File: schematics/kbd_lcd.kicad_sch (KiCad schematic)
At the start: 44 parts, among them J2 Mini-DIN-6, Q1 2N3906, U1 74HC04, U12 74HC04, U13 74HC125, U14 74HC14, U15 NE555P, U16 74HC04, U17 74HC595, U18 80x4 Character LCD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

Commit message: i can type lowercase! added tab key support and fixed cr and lf
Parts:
- removed R32: 10kΩ, symbol Device:R
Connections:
- net GND: now also R26.2, R27.1, R28.1
- net VCC: no longer R26.1, R27.1, R28.2
- net at U13.13, U14.5, U17.13 (~{OE})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: now also R28.2; no longer R28.1
- net at U20.18 (CB1): now also R26.1; no longer R26.2
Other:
- moved on the sheet: C5, C6, C9, D10, D11, D12, D3, D8, D9, J2, R15, R17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

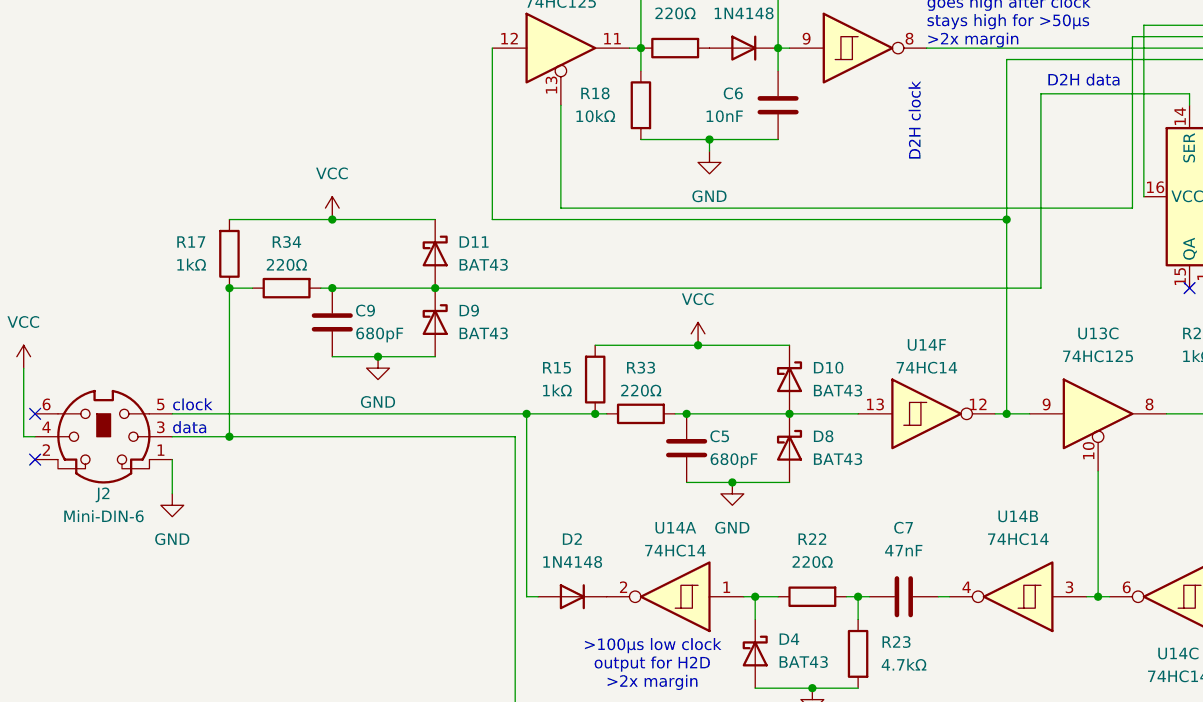
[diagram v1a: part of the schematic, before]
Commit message: trying to make it automatically hold reset during power-on. it's a little better
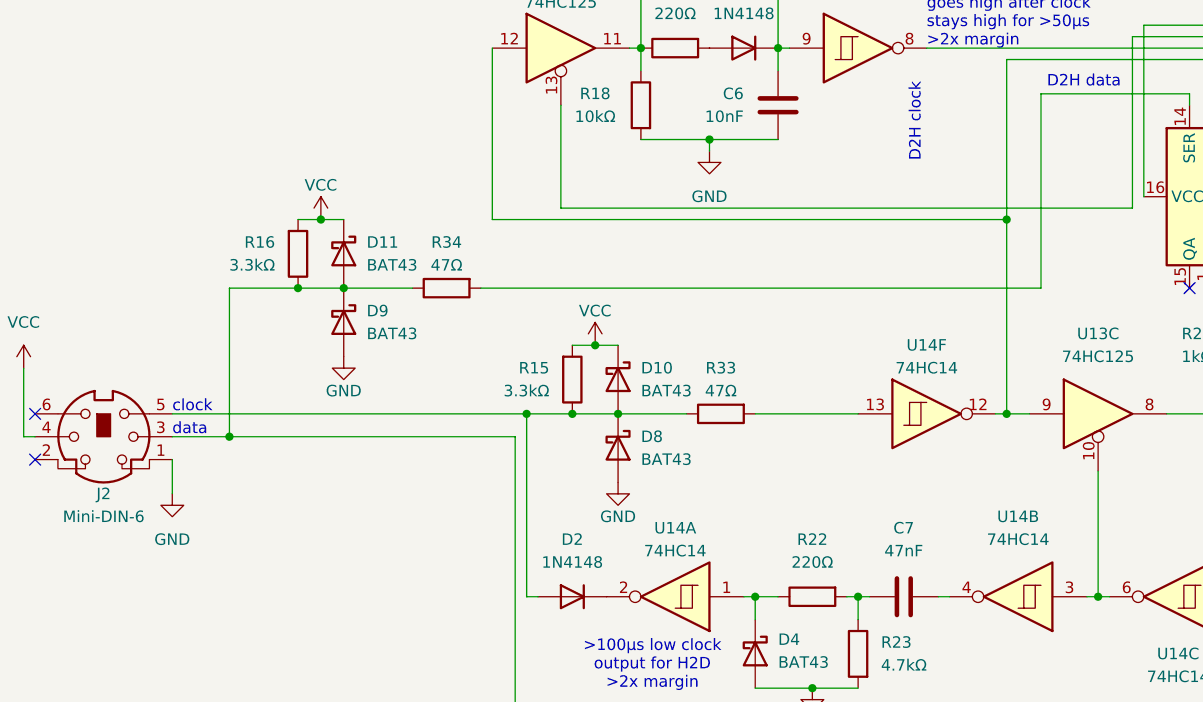
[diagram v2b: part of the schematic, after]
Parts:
- removed C5, C9: 680pF, symbol Device:C
- removed R17: 1kΩ, symbol Device:R
- added R16: 3.3kΩ, symbol Device:R
- R15: value 1kΩ -> 3.3kΩ
- R33, R34: value 220Ω -> 47Ω
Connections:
- net VCC: now also R16.2
- net at R33.2, U14.13: no longer D10.2 (A), D8.1 (K)
- net at D11.2 (A), D9.1 (K): now also D12.2 (A), J2.3, R34.1, R16.1; no longer R34.2, U17.14 (SER)
- net at D2.2 (A), J2.5, R15.1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: now also D10.2 (A), D8.1 (K)
- new net: R34.2, U17.14 (SER)
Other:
- moved on the sheet: R15, R33

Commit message: progress fixing caps lock led
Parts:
- added R31: 10kΩ, symbol Device:R
- R24: value 1kΩ -> 220Ω
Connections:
- net GND: now also R27.2; no longer R27.1, U14.11
- net VCC: now also R31.1
- net at U13.9, U14.12, U17.11 (SRCLK)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: no longer U13.12
- net at R33.2, U14.13: now also U13.12
- net at R18.1, R20.1, R21.1: now also U14.10; no longer U13.11
- net at U20.19 (CB2): now also R27.1; no longer R27.2
- new net: R31.2, U13.11, U14.11
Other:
- moved on the sheet: D11, D9, R16, R25, R26, R27, R34, U13D, U18

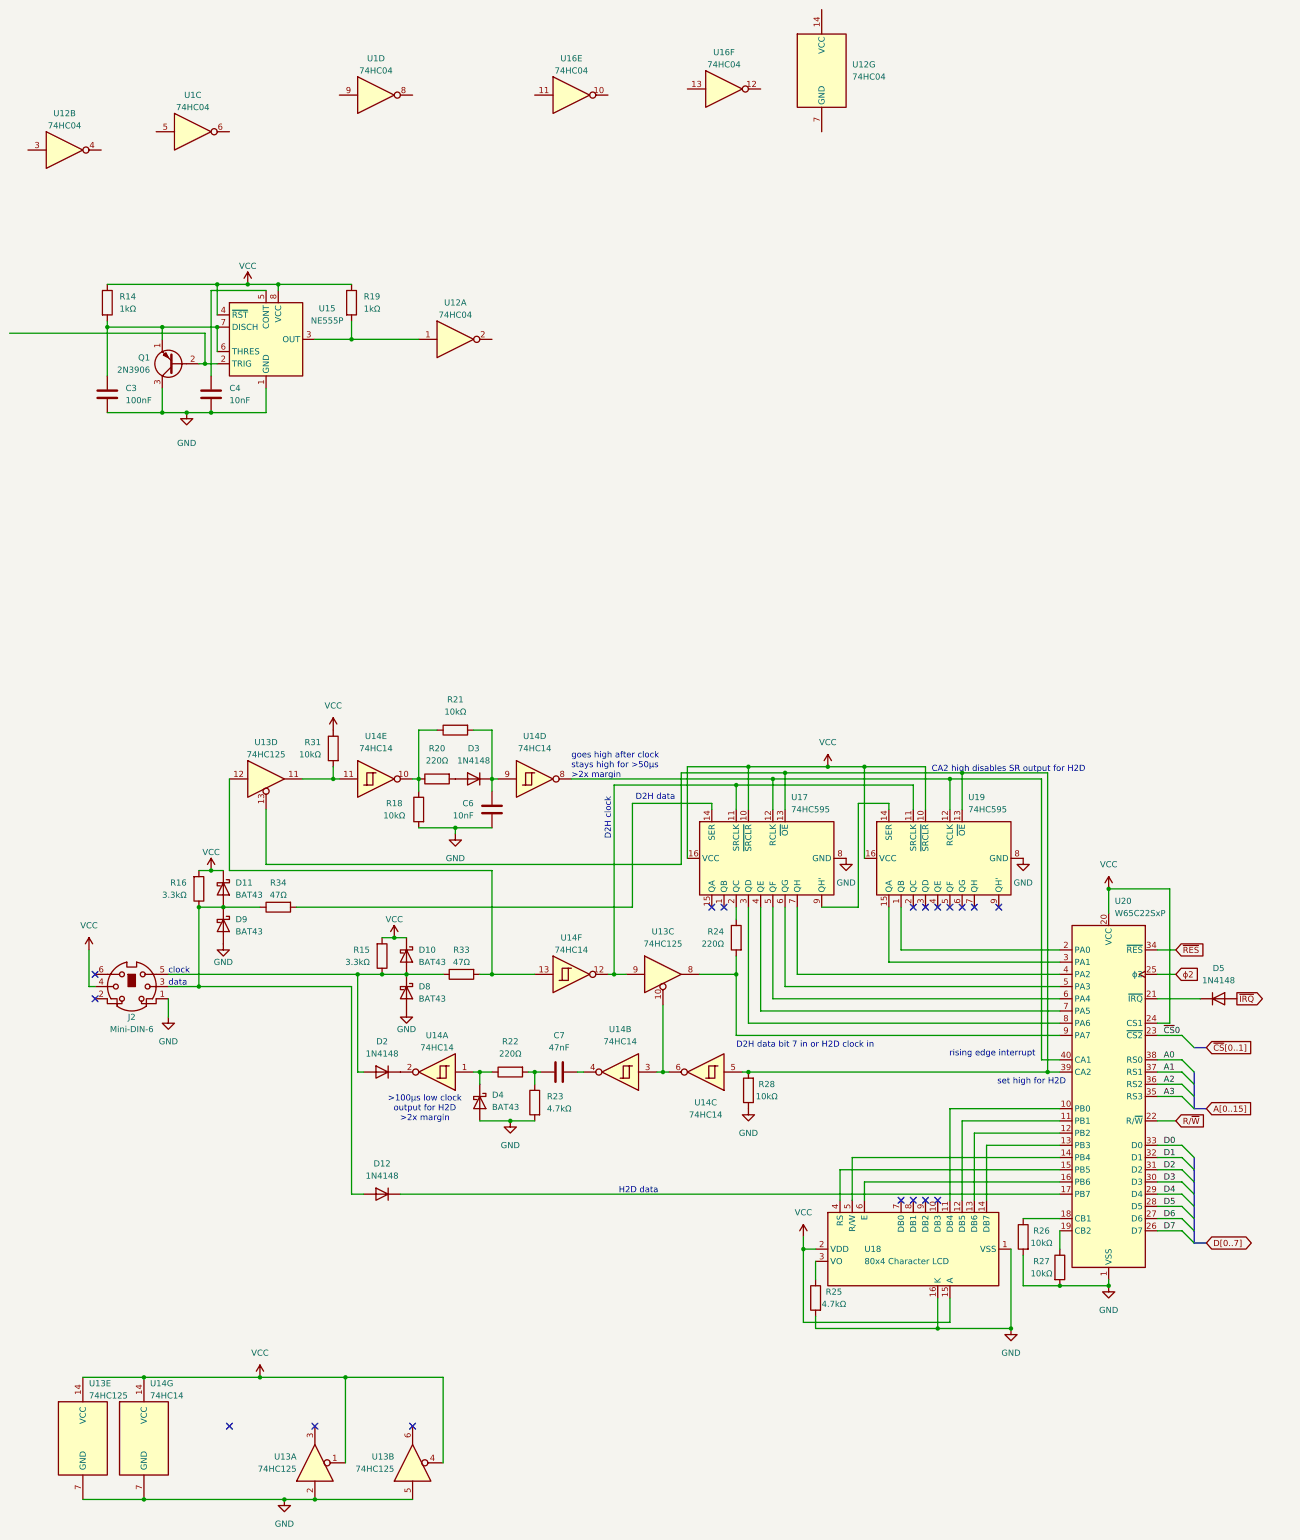
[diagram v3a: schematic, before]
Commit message: rewired the keyboard to remove 74HC245
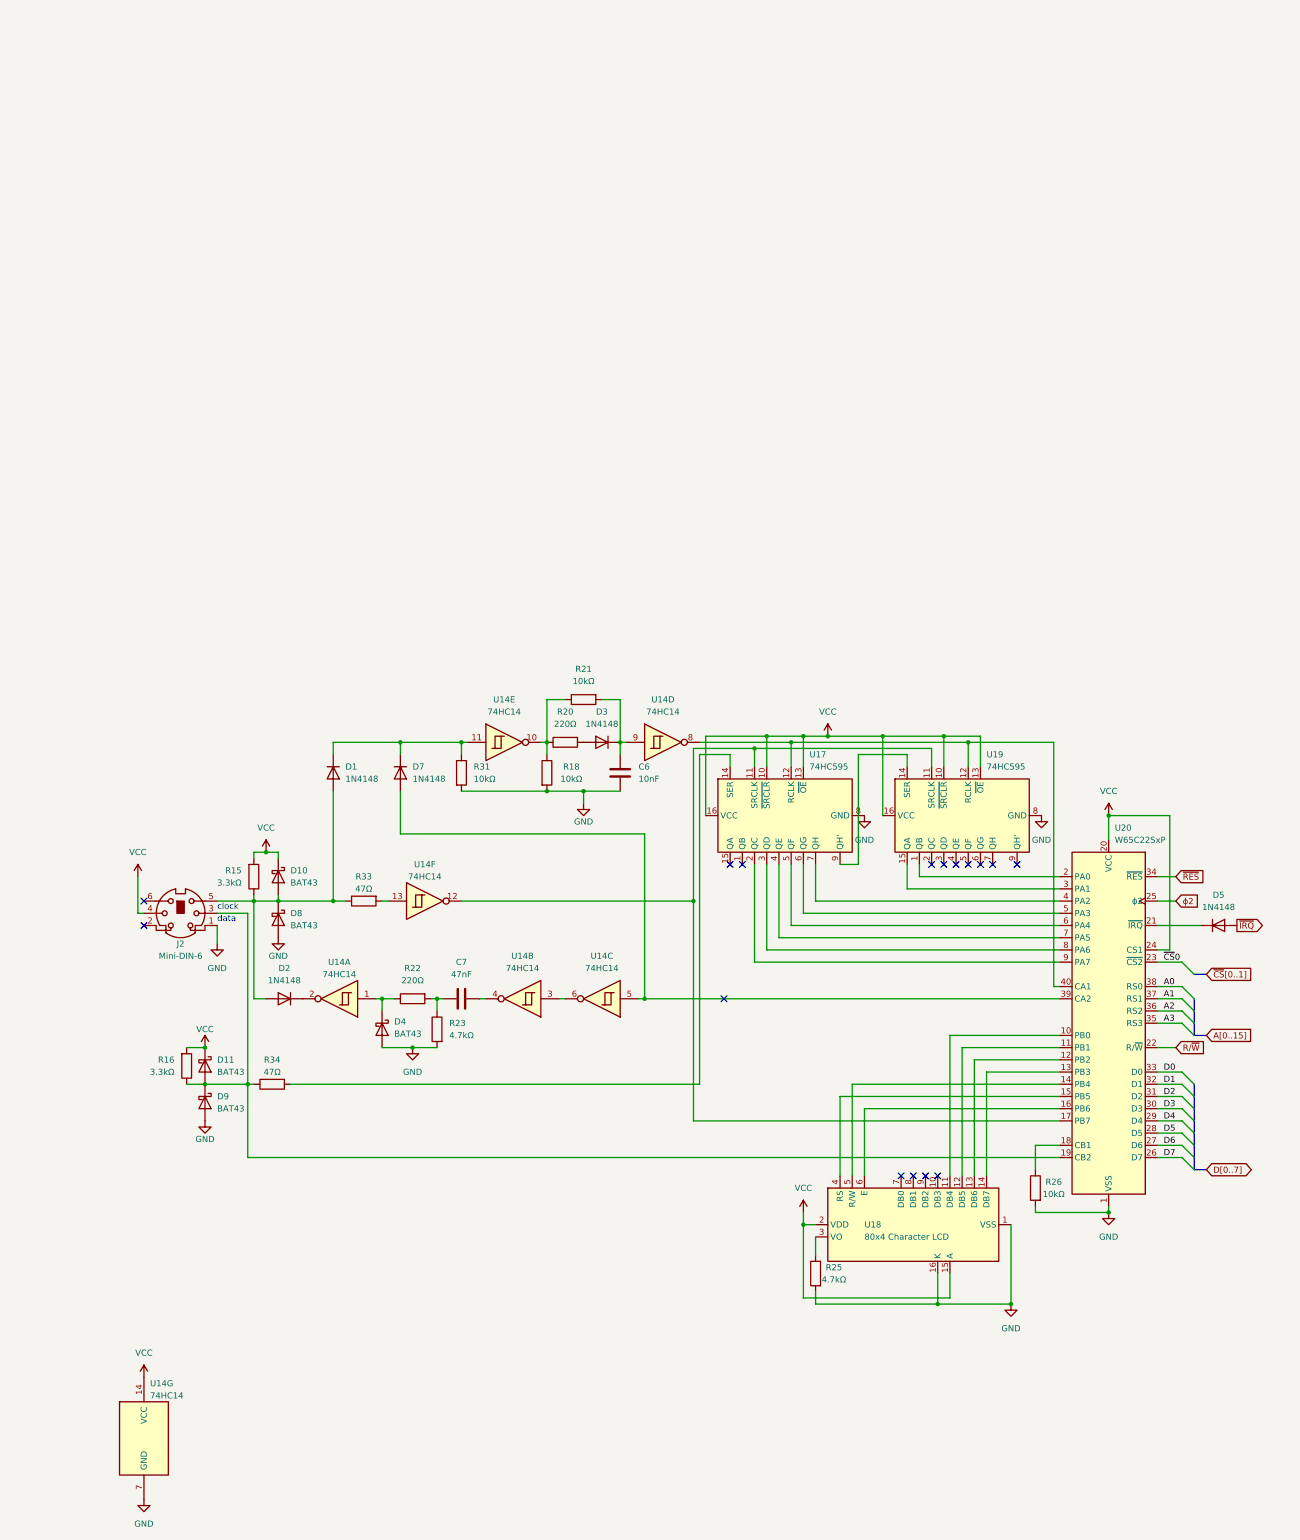
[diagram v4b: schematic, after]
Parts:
- removed C3: 100nF, symbol Device:C
- removed C4: 10nF, symbol Device:C
- removed D12: 1N4148, Diode_THT:D_DO-35_SOD27_P7.62mm_Horizontal, symbol Diode:1N4148
- removed Q1: 2N3906, Package_TO_SOT_THT:TO-92_Inline, symbol Transistor_BJT:2N3906
- removed R14, R19: 1kΩ, symbol Device:R
- removed R24: 220Ω, symbol Device:R
- removed R27, R28: 10kΩ, symbol Device:R
- removed U1, U12, U16: 74HC04, symbol 74xx:74HC04
- removed U13: 74HC125, symbol 74xx:74LS125
- removed U15: NE555P, Package_DIP:DIP-8_W7.62mm, symbol Timer:NE555P
- added D1, D7: 1N4148, Diode_THT:D_DO-35_SOD27_P7.62mm_Horizontal, symbol Diode:1N4148
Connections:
- net GND: now also R31.2
- net VCC: now also U17.13 (~{OE}), U19.13 (~{OE}); no longer R31.1
- net at D11.2 (A), D9.1 (K), J2.3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: now also U20.19 (CB2)
- net at U14.12, U17.11 (SRCLK), U19.11 (SRCLK): now also U20.17 (PB7)
- net at U14.11: now also R31.1, D1.1 (K), D7.1 (K); no longer R31.2
- net at U14.5, U20.39 (CA2): now also D7.2 (A); no longer U17.13 (~{OE}), U19.13 (~{OE})
- net at D10.2 (A), D2.2 (A), D8.1 (K)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: now also D1.2 (A)
- net at U20.9 (PA7): now also U17.2 (QC)
- no-connect marks 18 -> 16
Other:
- note removed: ">100µs low clock output for H2D >2x margin"
- note removed: "CA2 high disables SR output for H2D"
- note removed: "D2H clock"
- note removed: "D2H data"
- note removed: "D2H data bit 7 in or H2D clock in"
- note removed: "H2D data"
- note removed: "goes high after clock stays high for >50µs >2x margin"
- note removed: "rising edge interrupt"
- note removed: "set high for H2D"
- moved on the sheet: C6, C7, D10, D11, D2, D3, D4, D5, D8, D9, J2, R15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

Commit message: Address decoder pld file and no-VIA keyboard schematic and pld file.
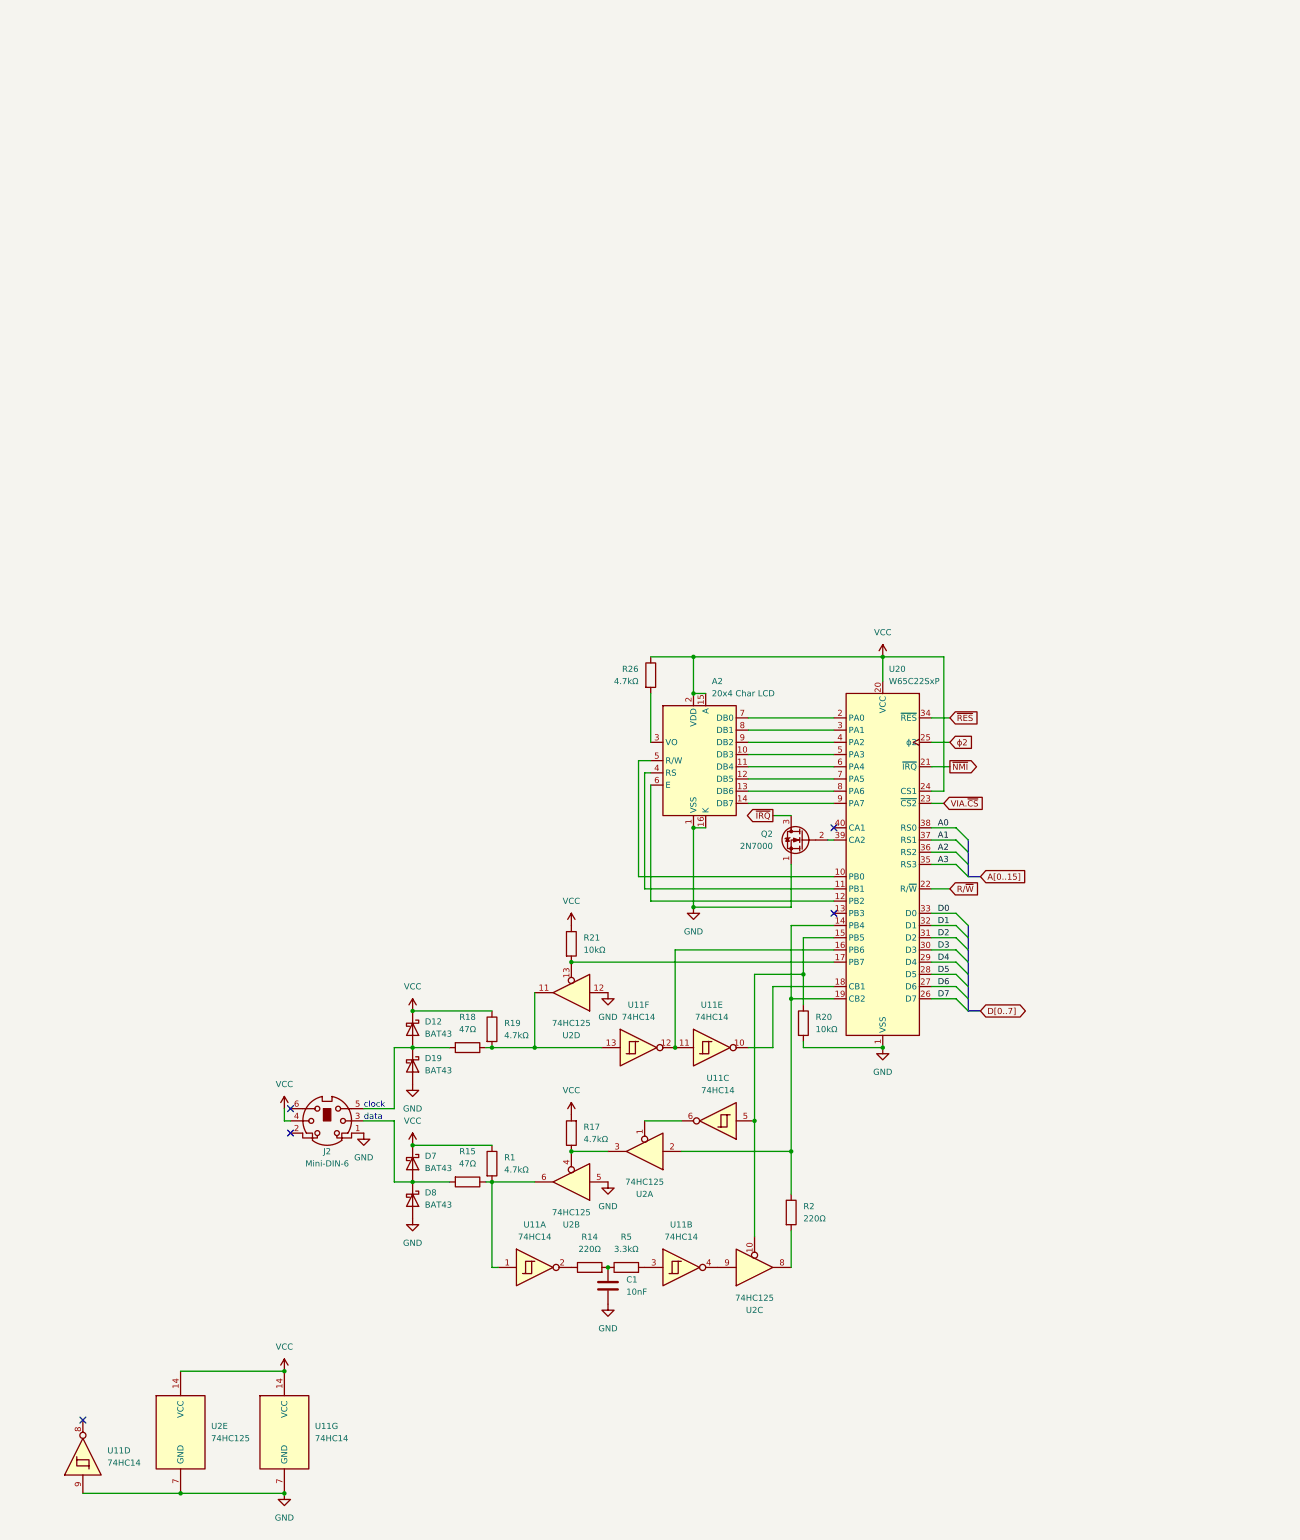
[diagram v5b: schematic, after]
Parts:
- removed C6: 10nF, symbol Device:C
- removed C7: 47nF, symbol Device:C
- removed D1, D2, D3, D5, D7: 1N4148, Diode_THT:D_DO-35_SOD27_P7.62mm_Horizontal, symbol Diode:1N4148
- removed D10, D11, D4, D9: BAT43, Diode_THT:D_DO-35_SOD27_P7.62mm_Horizontal, symbol Diode:BAT43
- removed R16: 3.3kΩ, symbol Device:R
- removed R22: 220Ω, symbol Device:R
- removed R23, R25: 4.7kΩ, symbol Device:R
- removed R31: 10kΩ, symbol Device:R
- removed R33, R34: 47Ω, symbol Device:R
- removed U14: 74HC14, symbol 74xx:74HC14
- removed U17, U19: 74HC595, symbol 74xx:74HC595
- added C1: 10nF, symbol Device:C
- added D12, D19, D7: BAT43, Diode_THT:D_DO-35_SOD27_P7.62mm_Horizontal, symbol Diode:BAT43
- added Q2: 2N7000, Package_TO_SOT_THT:TO-92_Inline, symbol Transistor_FET:2N7000
- added R1, R17, R19: 4.7kΩ, symbol Device:R
- added R14, R2: 220Ω, symbol Device:R
- added R5: 3.3kΩ, symbol Device:R
- added U11: 74HC14, symbol 74xx:74HC14
- added U2: 74HC125, symbol 74xx:74LS125
- A2: renamed from U18; value 80x4 Character LCD -> 20x4 Char LCD
- R15: value 3.3kΩ -> 47Ω
- R18: value 10kΩ -> 47Ω
- R20: value 220Ω -> 10kΩ
- R26: value 10kΩ -> 4.7kΩ
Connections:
- net GND: now also R20.2, C1.2, D19.2 (A), Q2.1 (S), U11.7 (GND), U11.9, U2.12, U2.5, U2.7 (GND); no longer R18.2, R26.2
- net VCC: now also R21.1, R26.1, D12.1 (K), D7.1 (K), R1.1, R17.2, R19.1, U11.14 (VCC), U2.14 (VCC); no longer R15.2
- net ~{IRQ}: now also Q2.3 (D)
- net at J2.3: now also D8.1 (K), R15.2, D7.2 (A); no longer U20.19 (CB2)
- net at U20.17 (PB7): now also R21.2, U2.13
- net at U20.39 (CA2): now also Q2.2 (G)
- net at A2.3 (VO): now also R26.2
- net at U20.10 (PB0): now also A2.5 (R/W); no longer A2.11 (DB4)
- net at U20.11 (PB1): now also A2.4 (RS); no longer A2.12 (DB5)
- net at U20.12 (PB2): now also A2.6 (E); no longer A2.13 (DB6)
- net at U20.13 (PB3): no longer A2.14 (DB7)
- net at U20.14 (PB4): now also U20.19 (CB2), R2.1, U2.2; no longer A2.5 (R/W)
- net at U20.15 (PB5): now also R20.1, U11.5, U2.10; no longer A2.4 (RS)
- net at U20.16 (PB6): now also U11.11, U11.12; no longer A2.6 (E)
- net at U20.18 (CB1): now also U11.10; no longer R26.1
- net at U20.2 (PA0): now also A2.7 (DB0)
- net ~{NMI}: now reaches U20.21 (~{IRQ})
- net at U20.3 (PA1): now also A2.8 (DB1)
- net at U20.4 (PA2): now also A2.9 (DB2)
- net at U20.5 (PA3): now also A2.10 (DB3)
- net at U20.6 (PA4): now also A2.11 (DB4)
- net at U20.7 (PA5): now also A2.12 (DB5)
- net at U20.8 (PA6): now also A2.13 (DB6)
- net at U20.9 (PA7): now also A2.14 (DB7)
- net ~{CS}0 renamed VIA.~{CS}
- new net: C1.1, R14.2, R5.1
- new net: R5.2, U11.3
- new net: R1.2, R15.1, U11.1, U2.6
- new net: R14.1, U11.2
- new net: R18.1, R19.2, U11.13, U2.11
- new net: D12.2 (A), D19.1 (K), J2.5, R18.2
- new net: R17.1, U2.3, U2.4
- new net: U11.6, U2.1
- new net: R2.2, U2.8
- new net: U11.4, U2.9
- no-connect marks 16 -> 5
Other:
- moved on the sheet: A2, U20
